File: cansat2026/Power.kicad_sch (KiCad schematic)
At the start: 34 parts, among them J201 FlightPin, J202 Heater, U201 TPS564252, U202 TPS564252, U203 TPS22810DBV

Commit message: Update: いろいろした
無線変えた
カメラのコネクタ変えた
i2cセンサ変えた
電源変えた:1.2V,3.8V,3.3V
IOエキスパンダ追加
FPGA追加
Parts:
- removed R203: 10k, Resistor_SMD:R_0402_1005Metric, symbol Device:R
- removed R205: 30k, Resistor_SMD:R_0603_1608Metric, symbol Device:R
- removed U201: TPS564252, Package_TO_SOT_SMD:SOT-563, symbol Project:TPS564252
- added C201, C213: 1uF, Capacitor_SMD:C_0402_1005Metric, symbol Device:C
- added C202: 2.2uF, Capacitor_SMD:C_0402_1005Metric, symbol Device:C
- added C203, C206: 10uF, Capacitor_SMD:C_0805_2012Metric, symbol Device:C
- added C204, C209: 100nF, Capacitor_SMD:C_0402_1005Metric, symbol Device:C
- added L202: 2.2uH, Inductor_SMD:L_Taiyo-Yuden_NR-50xx, symbol Device:L
- added R201: 39k, Resistor_SMD:R_0603_1608Metric, symbol Device:R
- added R202: 10k, Resistor_SMD:R_0402_1005Metric, symbol Device:R
- added U201: TPS70912, Package_TO_SOT_SMD:SOT-23-5, symbol Project:TPS70912DBV
- added U202: TPS561201, Package_TO_SOT_SMD:SOT-23-6, symbol Project:TPS561201
- added U203: TPS562242, Package_TO_SOT_SMD:SOT-563, symbol Project:TPS562242
- C208: renamed from C202; footprint Capacitor_SMD:C_0603_1608Metric -> Capacitor_SMD:C_0402_1005Metric; LCSC Part C14663 -> C307331
- C210: renamed from C203; value 30pF -> 33pF; LCSC Part C1570 -> C1562
- C215: renamed from C208; footprint Capacitor_SMD:C_0603_1608Metric -> Capacitor_SMD:C_0402_1005Metric; LCSC Part C14663 -> C307331
- C221: renamed from C214; footprint Capacitor_SMD:C_0603_1608Metric -> Capacitor_SMD:C_0402_1005Metric; LCSC Part C14663 -> C307331
- L201: value 3.3uH -> 4.7uH; footprint Inductor_SMD:L_TDK_VLS6045EX_VLS6045AF -> Inductor_SMD:L_Wuerth_PMCI-252012; DigiKey Part (none) -> WIP252012S-4R7MLDG; Mouser Part 810-VLS6045EX-3R3N -> (none)
- R203: renamed from R201; value 33k -> 3.9k; footprint Resistor_SMD:R_0402_1005Metric -> Resistor_SMD:R_0603_1608Metric; LCSC Part C25779 -> C23018
- R205: renamed from R204; value 12k -> 27k; footprint Resistor_SMD:R_0402_1005Metric -> Resistor_SMD:R_0603_1608Metric; LCSC Part C25752 -> C22967
- renumbered C201 to C207, C204 to C211, C206 to C212, C207 to C214, C209 to C216, C210 to C217, C211 to C218, C212 to C219, C213 to C220, C215 to C222, L202 to L203, R202 to R204, U202 to U204, U203 to U205
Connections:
- net 3V3: now also L202.2; no longer C205.1, L201.2
- net GND: now also C201.2, C202.2, C203.2, C206.2, C213.2, R202.2, U201.2 (GND), U202.1 (GND), U203.3 (GND)
- net VIN: now also C201.1, C203.1, C206.1, U201.1 (IN), U202.3 (VIN), U203.1 (VIN)
- net at L201.1: now also C204.1, U202.2 (SW)
- net at R204.2: now also C213.1, U203.5 (EN)
- net at C210.2, R205.2, R206.1: now also U203.6 (FB)
- new net: R201.2, R202.1, U202.4 (VFB)
- new net: C204.2, U202.6 (VBST)
- new net: C209.1, L202.1, U203.2 (SW)
- new net: C209.2, U203.4 (BST)
- new net 1.2V: C202.1, U201.5 (OUT)
- new net 3.8V: C205.1, L201.2, R201.1
- new net COM_P_EN: U202.5 (EN)
- no-connect marks 0 -> 1
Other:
- note added: "COM Power"
- note added: "FPGA Power"
- moved on the sheet: C207, C208, C210, C211, C212, R203, R204, R205, R206

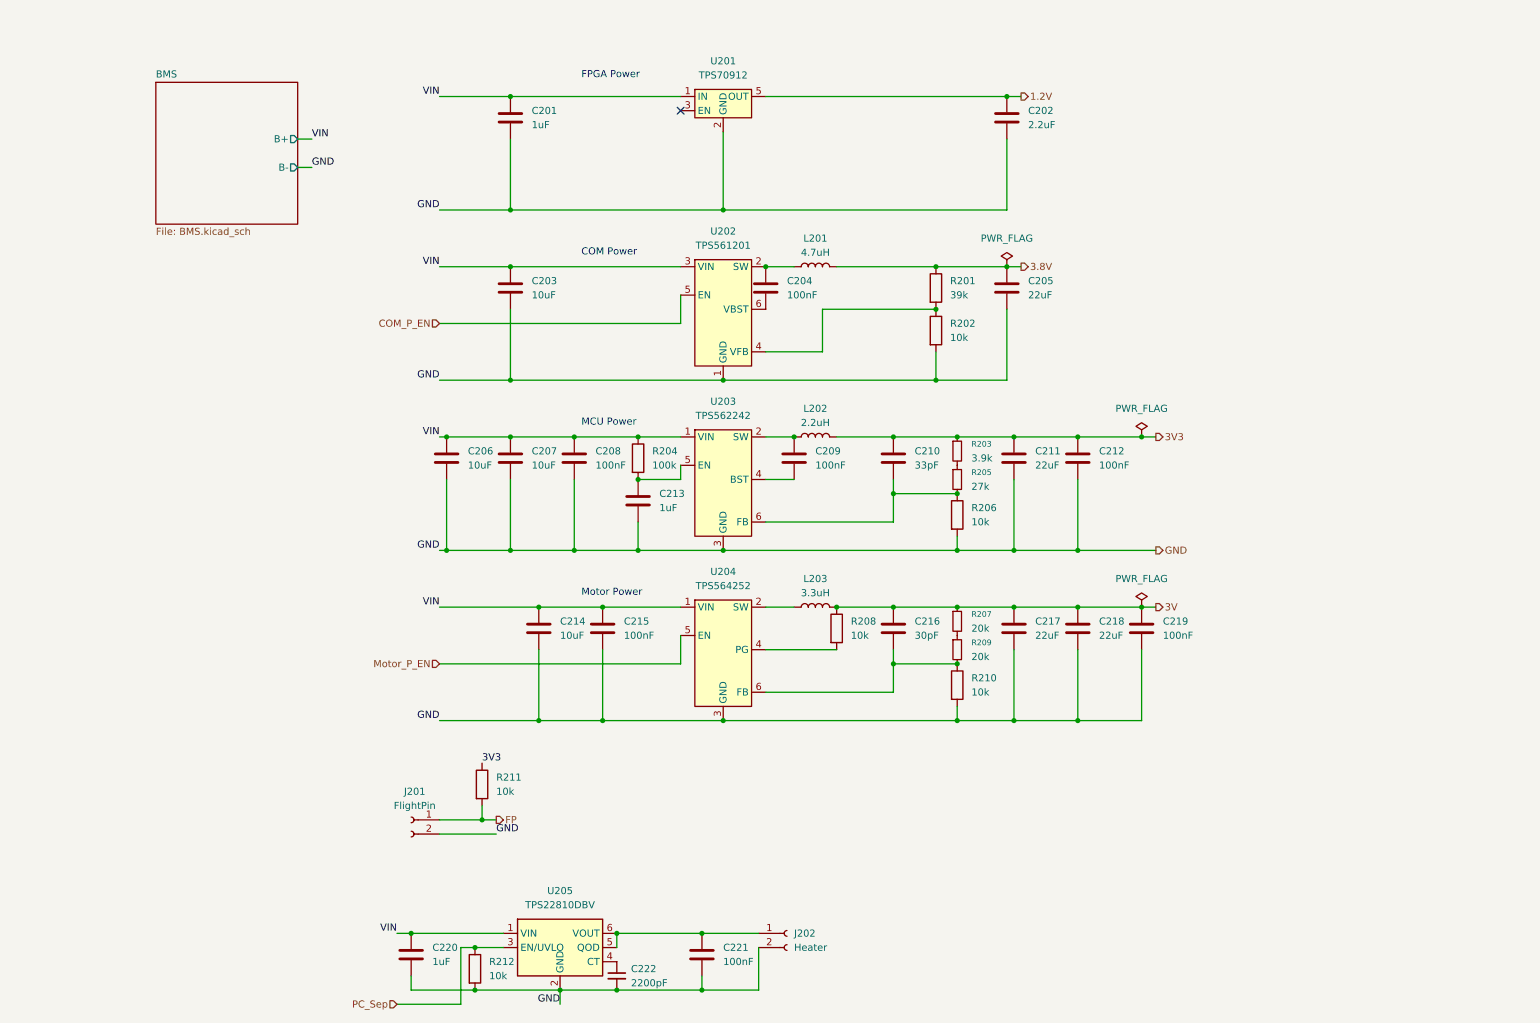
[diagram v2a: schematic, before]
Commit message: Update: MDと電源とか
MD変えた
モーター電源と主電源
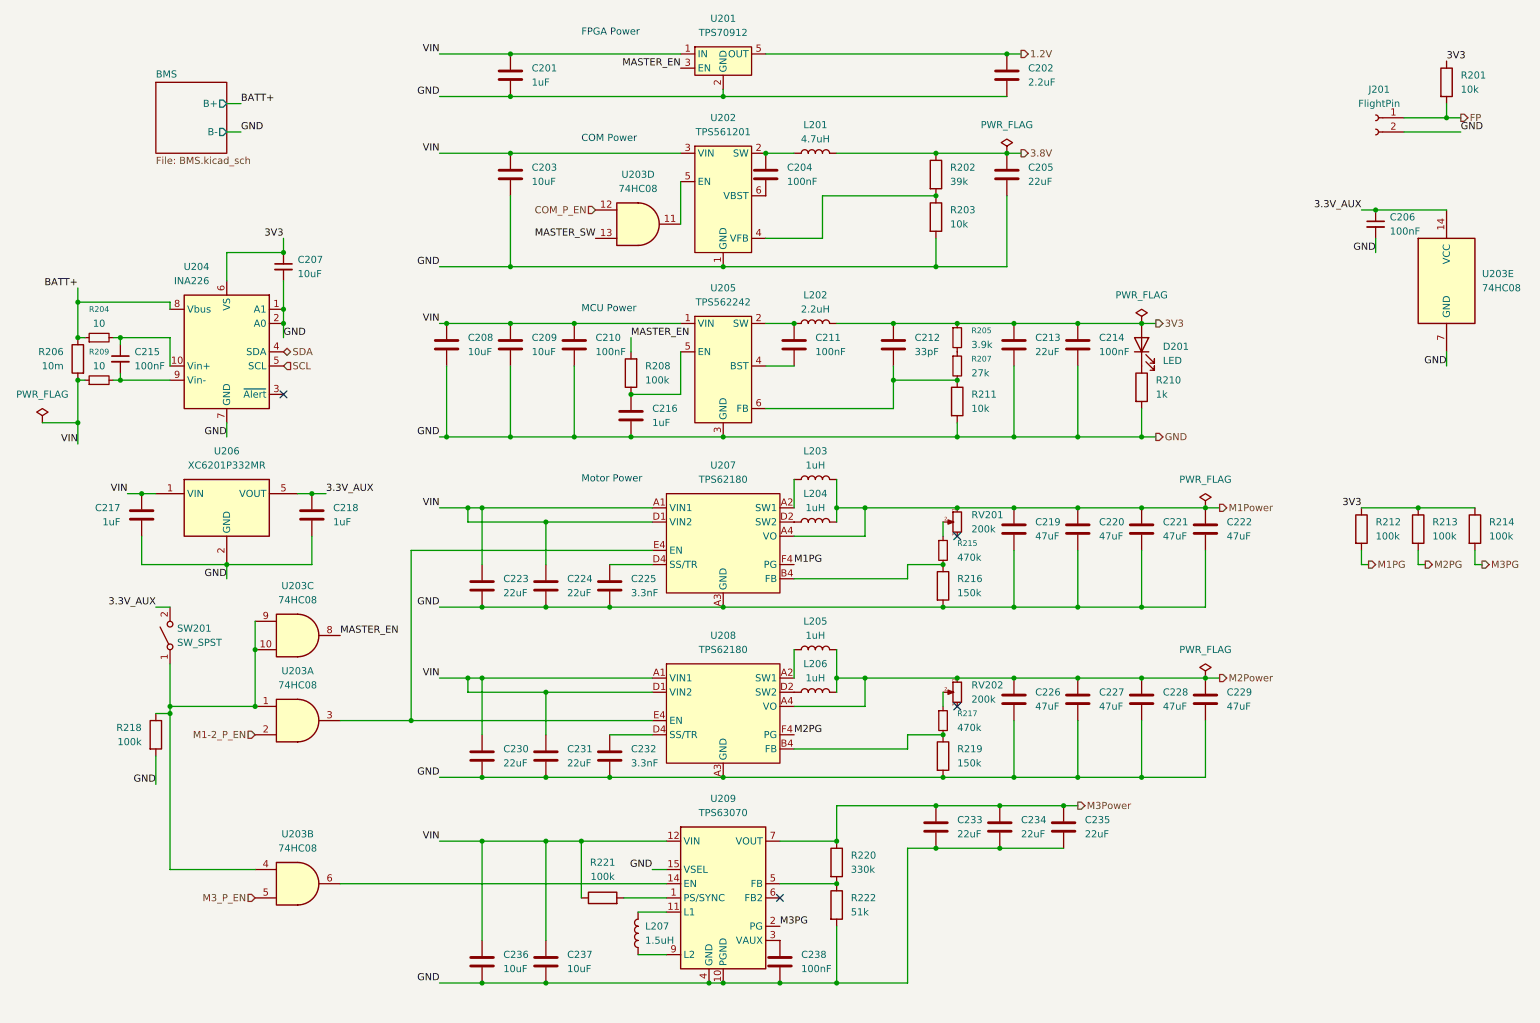
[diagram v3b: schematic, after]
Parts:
- removed C214: 10uF, Capacitor_SMD:C_0805_2012Metric, symbol Device:C
- removed C215: 100nF, Capacitor_SMD:C_0402_1005Metric, symbol Device:C
- removed C216: 30pF, Capacitor_SMD:C_0402_1005Metric, symbol Device:C
- removed C222: 2200pF, Capacitor_SMD:C_0402_1005Metric, symbol Device:C_Small
- removed J202: Heater, TerminalBlock_Phoenix:TerminalBlock_Phoenix_MKDS-1,5-2-5.08_1x02_P5.08mm_Horizontal, symbol Connector:Conn_01x02_Socket
- removed R204: 100k, Resistor_SMD:R_0402_1005Metric, symbol Device:R
- removed R207: 20k, Resistor_SMD:R_0402_1005Metric, symbol Device:R_Small
- removed U204: TPS564252, Package_TO_SOT_SMD:SOT-563, symbol Project:TPS564252
- removed U205: TPS22810DBV, Package_TO_SOT_SMD:SOT-23-6, symbol Project:TPS22810DBV
- added C206, C215: 100nF, Capacitor_SMD:C_0402_1005Metric, symbol Device:C_Small
- added C207: 10uF, Capacitor_SMD:C_0805_2012Metric, symbol Device:C_Small
- added C222, C226, C227, C228, C229: 47uF, Capacitor_SMD:C_0805_2012Metric, symbol Device:C
- added C223, C224, C230, C231, C233, C234, C235: 22uF, Capacitor_SMD:C_0805_2012Metric, symbol Device:C
- added C225, C232: 3.3nF, Capacitor_SMD:C_0603_1608Metric, symbol Device:C
- added C236, C237: 10uF, Capacitor_SMD:C_0805_2012Metric, symbol Device:C
- added C238: 100nF, Capacitor_SMD:C_0402_1005Metric, symbol Device:C
- added D201: LED, LED_SMD:LED_0603_1608Metric, symbol Device:LED
- added L204, L205, L206: 1uH, Inductor_SMD:L_Wuerth_PMCI-252010, symbol Device:L
- added L207: 1.5uH, Inductor_SMD:L_Wuerth_PMCI-201610, symbol Device:L
- added R204, R209: 10, Resistor_SMD:R_0402_1005Metric, symbol Device:R_Small
- added R206: 10m, Resistor_SMD:R_1206_3216Metric, symbol Device:R
- added R210: 1k, Resistor_SMD:R_0402_1005Metric, symbol Device:R
- added R213, R214, R218, R221: 100k, Resistor_SMD:R_0402_1005Metric, symbol Device:R
- added R217: 470k, Resistor_SMD:R_0603_1608Metric, symbol Device:R_Small
- added R219: 150k, Resistor_SMD:R_0603_1608Metric, symbol Device:R
- added R220: 330k, Resistor_SMD:R_0603_1608Metric, symbol Device:R
- added R222: 51k, Resistor_SMD:R_0402_1005Metric, symbol Device:R
- added RV201, RV202: 200k, Potentiometer_SMD:Potentiometer_Bourns_TC33X_Vertical, symbol Device:R_Potentiometer_Small
- added SW201: SW_SPST, Button_Switch_SMD:SW_DIP_SPSTx01_Slide_6.7x4.1mm_W8.61mm_P2.54mm_LowProfile, symbol Switch:SW_SPST
- added U203: 74HC08, Package_SO:SOIC-14_3.9x8.7mm_P1.27mm, symbol 74xx:74LS08
- added U204: INA226, Package_SO:TSSOP-10_3x3mm_P0.5mm, symbol Sensor_Energy:INA226
- added U206: XC6201P332MR, Package_TO_SOT_SMD:SOT-23-5, symbol Project:XC6201P332MR
- added U207, U208: TPS62180, Project:TPS62180YZF, symbol Project:TPS62180
- added U209: TPS63070, Project:QFN-16_2.4x2.9_Pitch0.5mm, symbol Project:TPS63070
- C204: LCSC Part C307331 -> C1525
- C210: renamed from C208; LCSC Part C307331 -> C1525
- C211: renamed from C209; LCSC Part C307331 -> C1525
- C217, C218: value 22uF -> 1uF; footprint Capacitor_SMD:C_0805_2012Metric -> Capacitor_SMD:C_0402_1005Metric; LCSC Part C45783 -> C52923
- C219: value 100nF -> 47uF; footprint Capacitor_SMD:C_0402_1005Metric -> Capacitor_SMD:C_0805_2012Metric; LCSC Part C1525 -> C16780
- C220: value 1uF -> 47uF; footprint Capacitor_SMD:C_0402_1005Metric -> Capacitor_SMD:C_0805_2012Metric; LCSC Part C52923 -> C16780
- C221: value 100nF -> 47uF; footprint Capacitor_SMD:C_0402_1005Metric -> Capacitor_SMD:C_0805_2012Metric; LCSC Part C307331 -> C16780
- L203: value 3.3uH -> 1uH; footprint Inductor_SMD:L_TDK_VLS6045EX_VLS6045AF -> Inductor_SMD:L_Wuerth_PMCI-252010; DigiKey Part (none) -> CIGT252010EH1R0MNE
- R208, R212: value 10k -> 100k; LCSC Part C25744 -> C25741
- R215: renamed from R209; value 20k -> 470k; footprint Resistor_SMD:R_0402_1005Metric -> Resistor_SMD:R_0603_1608Metric; LCSC Part C25765 -> C23178
- R216: renamed from R210; value 10k -> 150k; footprint Resistor_SMD:R_0402_1005Metric -> Resistor_SMD:R_0603_1608Metric; LCSC Part C25744 -> C22087
- renumbered C206 to C208, C207 to C209, C210 to C212, C211 to C213, C212 to C214, C213 to C216, R211 to R201, R201 to R202, R202 to R203, R203 to R205, R205 to R207, R206 to R211, U203 to U205
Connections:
- net PC_Sep is gone; now on net 3V3: R212.1
- net 3V3: now also C207.1, D201.2 (A), R213.1, R214.1, U204.6 (VS)
- net COM_P_EN: now also U203.12; no longer U202.5 (EN)
- net GND: now also C206.2, C207.2, C222.2, C223.2, C224.2, C225.2, C226.2, C227.2, C228.2, C229.2, C230.2, C231.2, C232.2, C233.2, C234.2, C235.2, C236.2, C237.2, C238.2, R210.2, R218.2, R219.2, R222.2, U203.7 (GND), U204.1 (A1), U204.2 (A0), U204.7 (GND), U206.2 (GND), U207.A3 (GND), U207.B3 (GND), U207.C3 (GND), U207.C4 (GND), U207.D3 (GND), U207.E3 (GND), U207.F3 (GND), U208.A3 (GND), U208.B3 (GND), U208.C3 (GND), U208.C4 (GND), U208.D3 (GND), U208.E3 (GND), U208.F3 (GND), U209.10 (PGND), U209.15 (VSEL), U209.4 (GND); no longer R212.2
- net VIN: now also C217.1, C223.1, C224.1, C230.1, C231.1, C236.1, C237.1, R206.2, R209.1, R221.1, U206.1 (VIN), U207.A1 (VIN1), U207.B1 (VIN1), U207.C1 (VIN1), U207.D1 (VIN2), U207.E1 (VIN2), U207.F1 (VIN2), U208.A1 (VIN1), U208.B1 (VIN1), U208.C1 (VIN1), U208.D1 (VIN2), U208.E1 (VIN2), U208.F1 (VIN2), U209.12 (VIN), U209.13 (VIN); no longer C220.1
- net MASTER_EN: now reaches R208.2
- net MASTER_EN: now also U201.3 (EN), U203.8
- net M1Power: now reaches C221.1
- net M1Power: now also C219.1, C220.1, L203.2, C222.1, L204.2, RV201.1, U207.A4 (VO)
- net at L203.1: now also U207.A2 (SW1), U207.B2 (SW1), U207.C2 (SW1)
- net at R215.2, R216.1: now also U207.B4 (FB)
- net at C216.1, U205.5 (EN): now also R208.1
- net at R215.1: now also RV201.2
- removed net 3V: C217.1, C218.1, C219.1, L203.2, R208.1
- new net: L206.1, U208.D2 (SW2), U208.E2 (SW2), U208.F2 (SW2)
- new net: U202.5 (EN), U203.11
- new net: R220.2, R222.1, U209.5 (FB)
- new net: R217.2, R219.1, U208.B4 (FB)
- new net: D201.1 (K), R210.1
- new net: R217.1, RV202.2
- new net: C215.1, R204.2, U204.10 (Vin+)
- new net: L205.1, U208.A2 (SW1), U208.B2 (SW1), U208.C2 (SW1)
- new net: C232.1, U208.D4 (SS/TR)
- new net: U203.3, U207.E4 (EN), U208.E4 (EN)
- new net: R221.2, U209.1 (PS/SYNC)
- new net: L207.2, U209.11 (L1)
- new net: U203.6, U209.14 (EN)
- new net: C238.1, U209.3 (VAUX)
- new net: L207.1, U209.9 (L2)
- new net: C215.2, R209.2, U204.9 (Vin-)
- new net: L204.1, U207.D2 (SW2), U207.E2 (SW2), U207.F2 (SW2)
- new net: C225.1, U207.D4 (SS/TR)
- new net: R218.1, SW201.1 (A), U203.1, U203.10, U203.4, U203.9
- new net: U206.3 (NC), U206.4 (NC)
- new net 3.3V_AUX: C206.1, C218.1, SW201.2 (B), U203.14 (VCC), U206.5 (VOUT)
- new net BATT+: R204.1, R206.1, U204.8 (Vbus)
- new net M1-2_P_EN: U203.2
- new net M1PG: R212.2, U207.F4 (PG)
- new net M2PG: R213.2, U208.F4 (PG)
- new net M2Power: C226.1, C227.1, C228.1, C229.1, L205.2, L206.2, RV202.1, U208.A4 (VO)
- new net M3PG: R214.2, U209.2 (PG)
- new net M3Power: C233.1, C234.1, C235.1, R220.1, U209.7 (VOUT), U209.8 (VOUT)
- new net M3_P_EN: U203.5
- new net MASTER_SW: U203.13
- new net SCL: U204.5 (SCL)
- new net SDA: U204.4 (SDA)
- no-connect marks 1 -> 4
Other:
- moved on the sheet: C201, C202, C203, C204, C205, C208, C209, C210, C211, C212, C213, C214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

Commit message: Update: いろいろした
GPS変えた
USB追加した
気圧センサ変えた
FPGA変えた
MDにキャパシタ追加した
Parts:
- U201: value TPS70912 -> TPS70912DRVR; footprint Package_TO_SOT_SMD:SOT-23-5 -> Package_SON:WSON-6-1EP_2x2mm_P0.65mm_EP1x1.6mm; symbol Project:TPS70912DBV -> Project:TPS70912DRV; LCSC Part (none) -> C2863472
- U202: value TPS561201 -> TPS561201DDC; LCSC Part (none) -> C220433
- U204: LCSC Part (none) -> C49851
- U205: LCSC Part (none) -> C19272253
- U207, U208, U209: now in the parts list
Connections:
- net 1.2V: now also U201.1 (OUT); no longer U201.5 (OUT)
- net GND: now also U201.3 (GND), U201.7 (GND); no longer U201.2 (GND)
- net MASTER_EN: now also U201.4 (EN); no longer U201.3 (EN)
- net MASTER_SW: now also R218.1, SW201.1 (A), U203.1, U203.10, U203.4, U203.9
- net VIN: now also U201.6 (IN); no longer U201.1 (IN)
- new net: U201.2 (NC), U201.5 (NC)

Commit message: Update: 完成した
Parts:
- removed U206: XC6201P332MR, Package_TO_SOT_SMD:SOT-23-5, symbol Project:XC6201P332MR
- added C203, C204: 100nF, Capacitor_SMD:C_0402_1005Metric, symbol Device:C
- added C235: 10uF, Capacitor_SMD:C_0805_2012Metric, symbol Device:C
- added U202: TCR2LN18, Project:SDFN4, symbol Project:TCR2LN18
- added U207: XC6206P332MR, Package_TO_SOT_SMD:SOT-23-3, symbol Regulator_Linear:XC6206PxxxMR
- C209: renamed from C207; footprint Capacitor_SMD:C_0805_2012Metric -> Capacitor_SMD:C_0402_1005Metric; LCSC Part C15850 -> C15525
- J201: 秋月 Part (none) -> 112247
- L202: Mouser Part (none) -> 963-LSXND5050WDL2R2N
- R202: footprint Resistor_SMD:R_0603_1608Metric -> Resistor_SMD:R_0402_1005Metric; LCSC Part C25153 -> C25783
- R205: value 3.9k -> 15k; footprint Resistor_SMD:R_0603_1608Metric -> Resistor_SMD:R_0402_1005Metric; LCSC Part C23018 -> C25756
- R207: value 27k -> 47k; footprint Resistor_SMD:R_0603_1608Metric -> Resistor_SMD:R_0402_1005Metric; LCSC Part C22967 -> C25792
- R211: value 10k -> 20k; LCSC Part C25744 -> C25765
- R215, R217: footprint Resistor_SMD:R_0603_1608Metric -> Resistor_SMD:R_0402_1005Metric; LCSC Part C23178 -> C25790
- R216, R219: footprint Resistor_SMD:R_0603_1608Metric -> Resistor_SMD:R_0402_1005Metric; LCSC Part C22087 -> C25774
- R220: footprint Resistor_SMD:R_0603_1608Metric -> Resistor_SMD:R_0402_1005Metric; LCSC Part C23137 -> C25778
- U208: renamed from U207; LCSC Part (none) -> C2071394
- U209: renamed from U208; LCSC Part (none) -> C2071394
- U210: renamed from U209; LCSC Part (none) -> C2072046
- renumbered C203 to C205, C204 to C206, C205 to C207, C206 to C208, C208 to C210, C209 to C211, C210 to C212, C211 to C213, C212 to C214, C213 to C215, C214 to C216, C215 to C217, C216 to C218, C217 to C219, C218 to C220, C219 to C221, C220 to C222, C221 to C223, C222 to C224, C223 to C225, C224 to C226, C225 to C227, C226 to C228, C227 to C229, C228 to C230, C229 to C231, C230 to C232, C231 to C233, C232 to C234, C233 to C236, C234 to C237, C235 to C238, C236 to C239, C237 to C240, C238 to C241, U202 to U203, U203 to U204, U204 to U205, U205 to U206
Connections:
- net 3.3V_AUX: now also U207.2 (VO)
- net 3V3: now also C203.1, U202.3 (CTRL), U202.4 (VIN)
- net GND: now also C203.2, C204.2, C235.2, U202.2 (GND), U207.1 (GND)
- net M1-2_P_EN: now also U204.1; no longer U204.2
- net M3Power: now also C235.1
- net M3_P_EN: now also U204.4; no longer U204.5
- net MASTER_SW: now also U204.2, U204.5; no longer U204.1, U204.4
- net VIN: now also U207.3 (VI)
- new net 1.8V: C204.1, U202.1 (VOUT)
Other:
- moved on the sheet: C236, C237, C238
